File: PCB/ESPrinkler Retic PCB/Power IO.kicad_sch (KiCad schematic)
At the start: 32 parts, among them J6 Conn_01x04, Q1 AO3400A, Q2 AO3400A, U1 TPS5430DDA

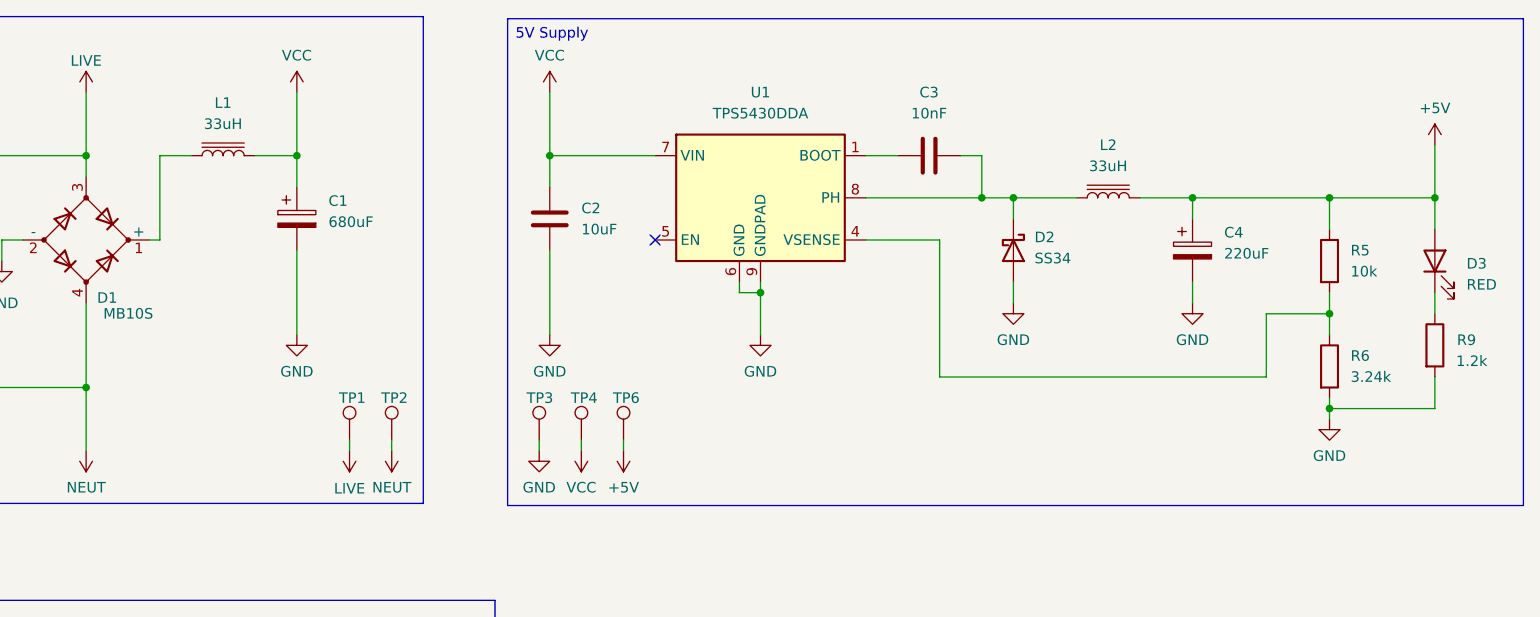
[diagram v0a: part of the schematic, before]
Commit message: Change DC-DC converter & PCB routing
Previous DC-DC converter max input voltage was close to VIN. Changed out for 40V rated input, and a simpler design.

Also re-routed 5V rail to top layer to reduce layer swapping using vias for power lines
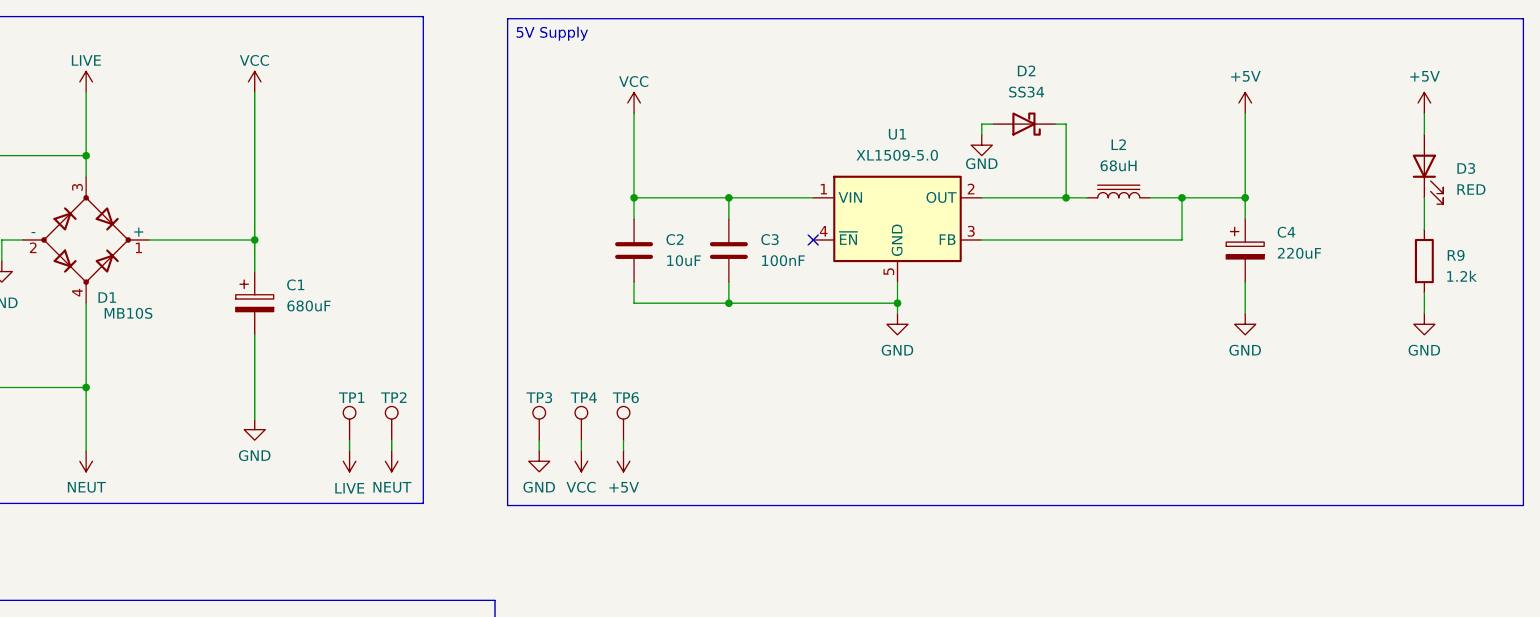
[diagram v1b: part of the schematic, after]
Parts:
- removed L1: 33uH, Inductor_SMD:L_APV_ANR5045, symbol Device:L_Iron
- removed R5: 10k, Resistor_SMD:R_0805_2012Metric, symbol Device:R
- removed R6: 3.24k, Resistor_SMD:R_0805_2012Metric, symbol Device:R
- removed U1: TPS5430DDA, Package_SO:TI_SO-PowerPAD-8_ThermalVias, symbol Regulator_Switching:TPS5430DDA
- added U1: XL1509-5.0, Package_SO:SOIC-8_3.9x4.9mm_P1.27mm, symbol Regulator_Switching:XL1509-5.0
- C3: value 10nF -> 100nF; Manufacturer P/N CL21B103KBANNNC -> CL21B104KCFNNNE; Supplier P/N C1710 -> C28233
- L2: value 33uH -> 68uH; Manufacturer P/N SMNR5040-330MT -> SMNR5040-680MT; Supplier P/N C9390 -> C9393
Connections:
- net +5V: now also U1.3 (FB)
- net GND: now also C3.1, U1.5 (GND), U1.6 (GND), U1.7 (GND), U1.8 (GND)
- net VCC: now also C3.2, D1.1 (+), U1.1 (VIN)
- net at D2.1 (K), L2.1: now also U1.2 (OUT); no longer C3.2
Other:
- moved on the sheet: C1, C2, C3, C4, D2, D3, L2, R9

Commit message: Add TVS protection
Added SMAJ33A TVS on VCC
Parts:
- added D22: SMAJ33A, Diode_SMD:D_SMA, symbol Diode:SMAJ33A
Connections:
- net GND: now also D22.2 (A2)
- net VCC: now also D22.1 (A1)
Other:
- moved on the sheet: C2, C3, C4, D2, D3, F2, L2, R9, TP1, TP2, TP3, TP4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

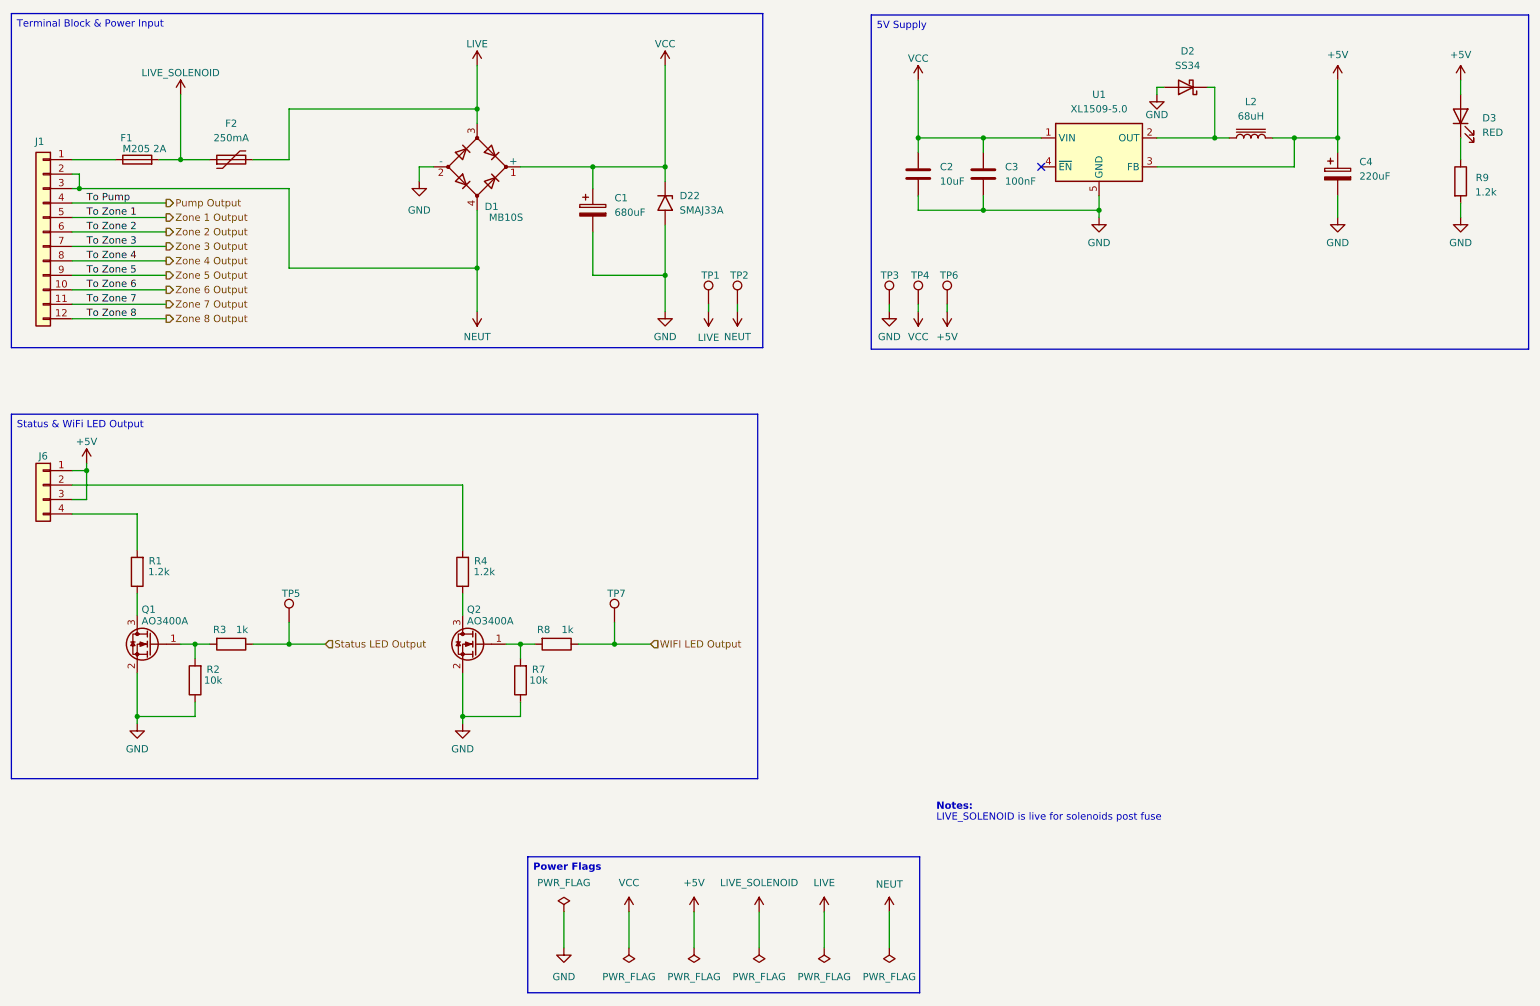
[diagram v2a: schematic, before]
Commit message: Labelling as V2.0
Repo needs to change, I have been using it poorly. V2.0 will be the next "main branch". After that, forks will be used instead

Also in this commit, I have updated the custom footprints and updated the links to them in the project.
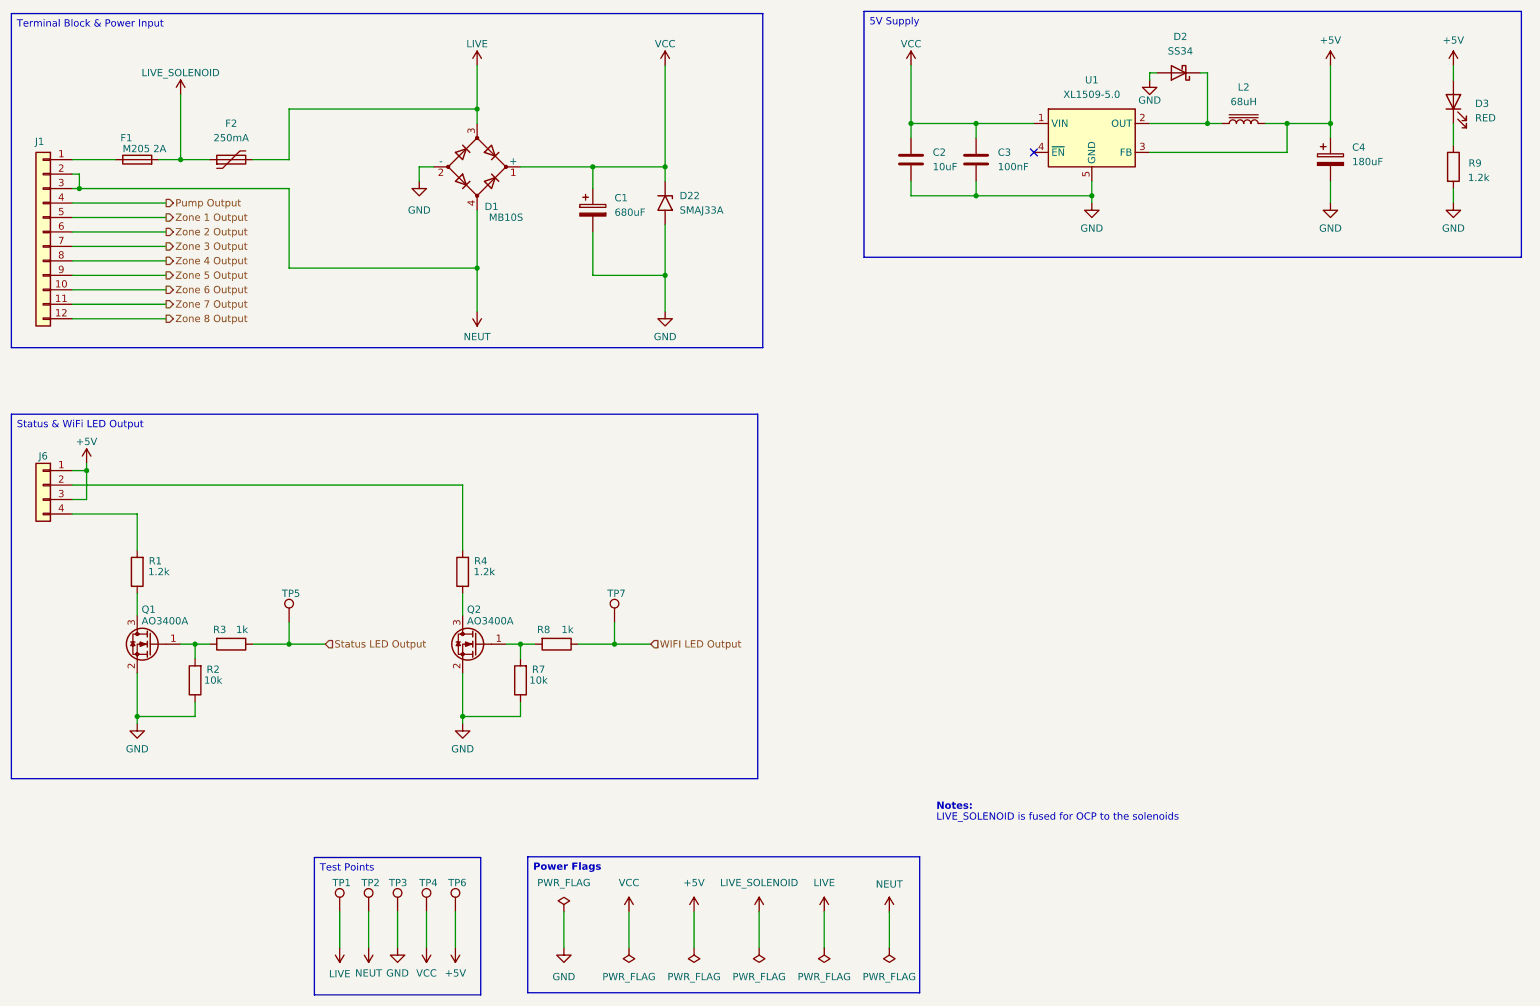
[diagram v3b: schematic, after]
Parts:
- C4: value 220uF -> 180uF; Manufacturer CX(Dongguan Chengxing Elec) -> Ymin; Manufacturer P/N GR227M010E11RR0VH4FP0 -> LKMC0901E181MF; Supplier P/N C2036 -> C442817
- D1: footprint Package_SO:OnSemi_751EP_SOIC-4_3.9x4.725mm_P2.54mm -> Footprints:OnSemi_751EP_SOIC-4_3.9x4.725mm_P2.54mm
- U1: Manufacturer (none) -> XLSEMI; Manufacturer P/N (none) -> XL1509-5.0E1; Supplier (none) -> LCSC; Supplier P/N (none) -> C61063
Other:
- note added: "LIVE_SOLENOID is fused for OCP to the solenoids"
- note removed: "LIVE_SOLENOID is live for solenoids post fuse"
- moved on the sheet: C2, C3, C4, D2, D3, L2, R9, TP1, TP2, TP3, TP4, TP6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

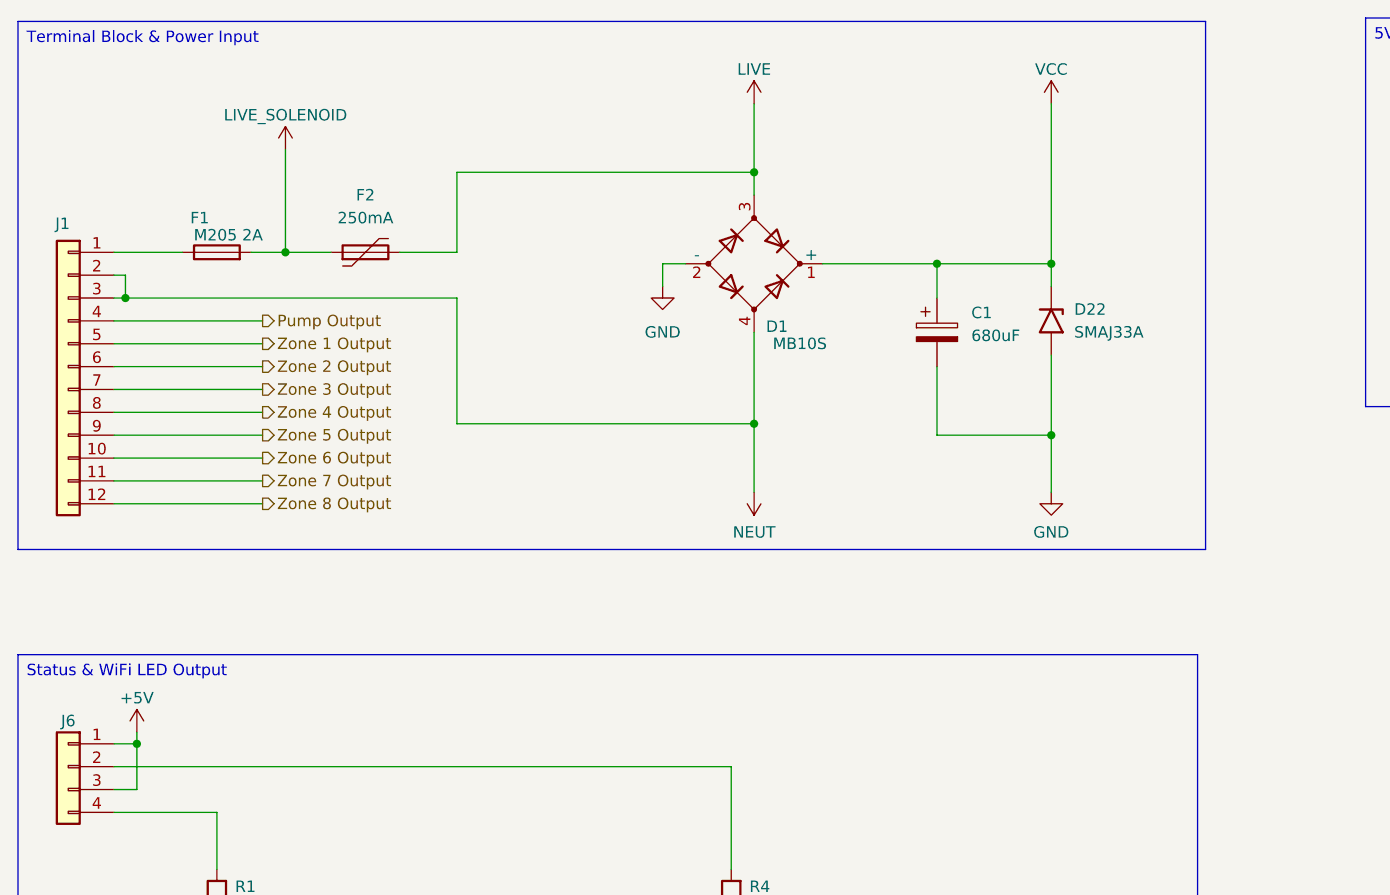
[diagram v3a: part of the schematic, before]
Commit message: Change 12-pin connector
Change from screw terminal barrier block to a wire-to-board screw terminal block.

Opted for a 3-pin terminal block, 4 of them due the 12-pin not being available through lcsc, to get a total of 12 when connected together. Makes the design a bit confusing but the BOM is accurate
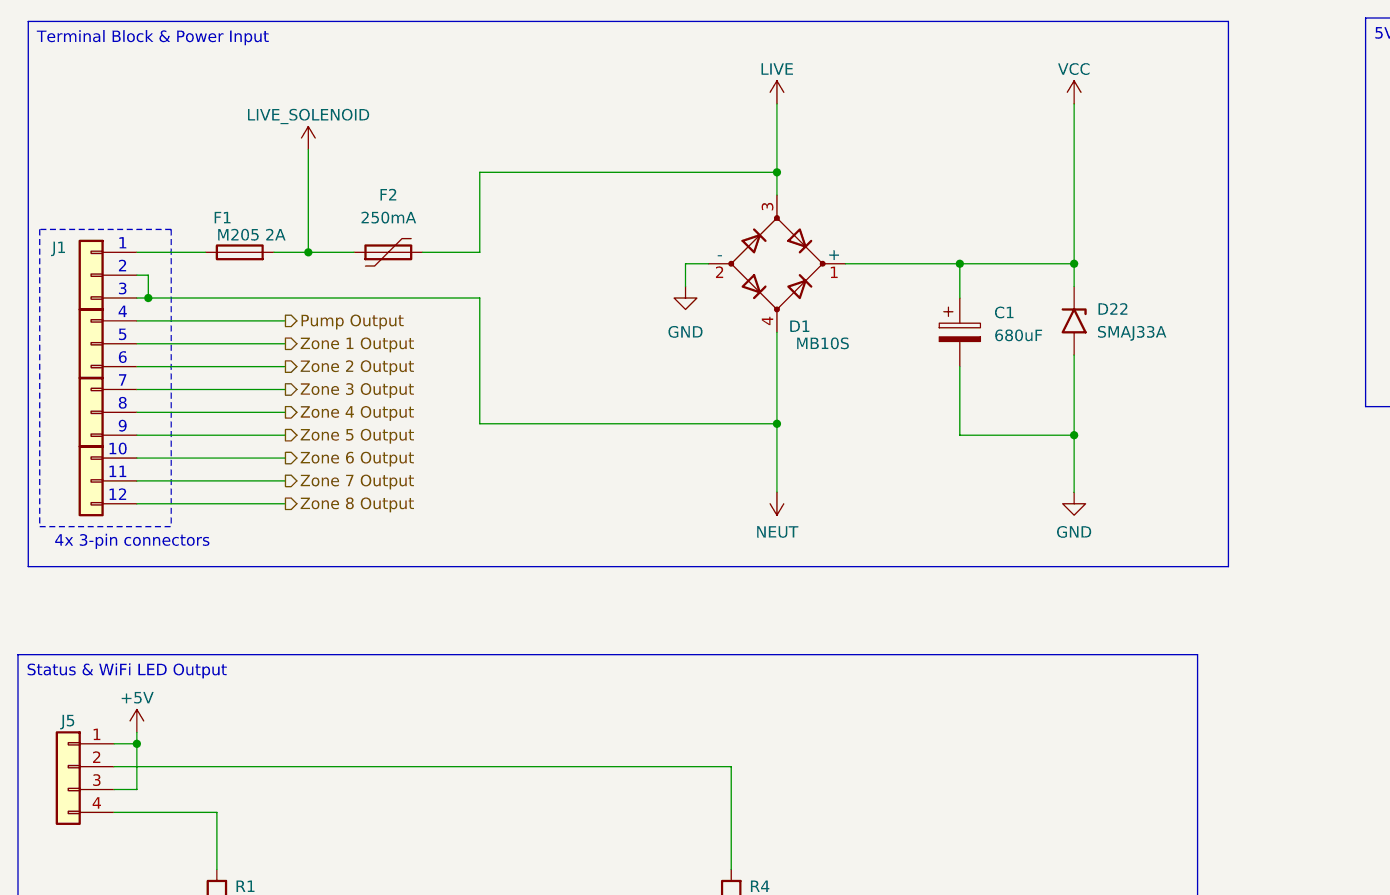
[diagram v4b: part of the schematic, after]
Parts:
- removed J1: (no value), Footprints:DBT30C-7.62-12P-BK-P, symbol Connector_Generic:Conn_01x12
- added J1, J2, J3, J4: DB910-7.62-3P-GN-S, Footprints:DORABO_DB910-7.62-3P-GN-S_1x03_P7.62mm_Vertical, symbol Connector_Generic:Conn_01x03
- renumbered J6 to J5
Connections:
- net NEUT: now also J1.2 (Pin_2), J1.3 (Pin_3)
- net Pump Output: now also J2.1 (Pin_1)
- net Zone 1 Output: now also J2.2 (Pin_2)
- net Zone 2 Output: now also J2.3 (Pin_3)
- net Zone 3 Output: now also J3.1 (Pin_1)
- net Zone 4 Output: now also J3.2 (Pin_2)
- net Zone 5 Output: now also J3.3 (Pin_3)
- net Zone 6 Output: now also J4.1 (Pin_1)
- net Zone 7 Output: now also J4.2 (Pin_2)
- net Zone 8 Output: now also J4.3 (Pin_3)
- net at F1.1: now also J1.1 (Pin_1)
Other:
- note added: "1"
- note added: "10"
- note added: "11"
- note added: "12"
- note added: "2"
- note added: "3"
- note added: "4"
- note added: "4x 3-pin connectors"
- note added: "5"
- note added: "6"
- note added: "7"
- note added: "8"
- note added: "9"
- moved on the sheet: C1, D1, D22, F1, F2

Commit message: Edit BOM and silkscreen
Getting ready to make production files
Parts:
- D22: Manufacturer (none) -> Littelfuse; Manufacturer P/N (none) -> SMAJ33A; Supplier (none) -> LCSC; Supplier P/N (none) -> C223988
